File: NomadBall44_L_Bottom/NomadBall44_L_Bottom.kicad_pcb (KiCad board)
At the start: 2 copper layers, 149 x 96.5 mm, 58 parts, among them SW1 SW_Push, SW10 SW_Push, SW11 SW_Push, SW12 SW_Push, SW13 SW_Push, SW14 SW_Push, SW15 SW_Push, SW16 SW_Push, SW17 SW_Push, SW18 SW_Push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

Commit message: ボトムプレートを作成
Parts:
- removed BT1: Battery_Cell, NomadBall44:JST_S2B-PH-SM4-TB
- removed D1, D10, D11, D12, D13, D14, D15, D16, D17, D18, D19, D2, D20, D21, D22, D23, D3, D4, D5, D6, D7, D8, D9: D, NomadBall44:Diode_SMD
- removed SW1, SW10, SW11, SW12, SW13, SW14, SW15, SW16, SW17, SW18, SW2, SW22, SW23, SW3, SW4, SW5, SW6, SW7, SW8, SW9: SW_Push, NomadBall44:Choc_v2_Hotswap_1u
- removed SW19, SW20, SW21: SW_Push, NomadBall44:Kailh_Choc_V1_Hotswap_thin_via
- removed SW24: SW_SPDT, NomadBall44:TGSW_MSK-12D19
- removed U1: XIAO-nRF52840-Plus-SMD, NomadBall44:XIAO-nRF52840-Plus-ver2
- REF** (x9): value MountingHole_4.3mm_M4 -> Val**; footprint MountingHole:MountingHole_4.3mm_M4 -> NomadBall44:m2_Screw_Hole_EdgeCuts
- moved REF** 79.6 mm to (74.0, 73.3)
- moved REF** 79.6 mm to (152.2, 108.1)
- moved REF** 79.6 mm to (73.9, 100.1)
- moved REF** 79.6 mm to (91.6, 111.6)
- moved REF** 79.6 mm to (152.0, 66.5)
- moved REF** 79.6 mm to (112.3, 50.8)
- moved REF** 79.6 mm to (152.0, 86.0)
- moved REF** 79.6 mm to (112.1, 99.9)
- moved REF** 79.6 mm to (179.7, 121.6)
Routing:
- net Row3: track 230.2 -> 0.00 mm, vias 15 -> 0
- net Col5: track 212.8 -> 0.00 mm, vias 9 -> 0
- net Row1: track 190.7 -> 0.00 mm, vias 21 -> 0
- net Row2: track 179.8 -> 0.00 mm, vias 14 -> 0
- net Row0: track 171.8 -> 0.00 mm, vias 12 -> 0
- net Col4: track 170.4 -> 0.00 mm, vias 1 -> 0
- net Col2: track 167.8 -> 0.00 mm, vias 7 -> 0
- net Col1: track 154.1 -> 0.00 mm, vias 11 -> 0
- net Col3: track 154.1 -> 0.00 mm, vias 3 -> 0
- net Col0: track 131.7 -> 0.00 mm, vias 9 -> 0
- net GND: track 47.4 -> 0.00 mm, vias 5 -> 0
- net Net-(BT1--): track 19.2 -> 0.00 mm, vias 1 -> 0
- net Net-(D1-A): track 19.1 -> 0.00 mm, vias 2 -> 0
- net Net-(D5-A): track 19.1 -> 0.00 mm, vias 2 -> 0
- net Net-(D2-A): track 19.1 -> 0.00 mm, vias 2 -> 0
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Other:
- board size 149 x 96.5 mm -> 149 x 93.1 mm

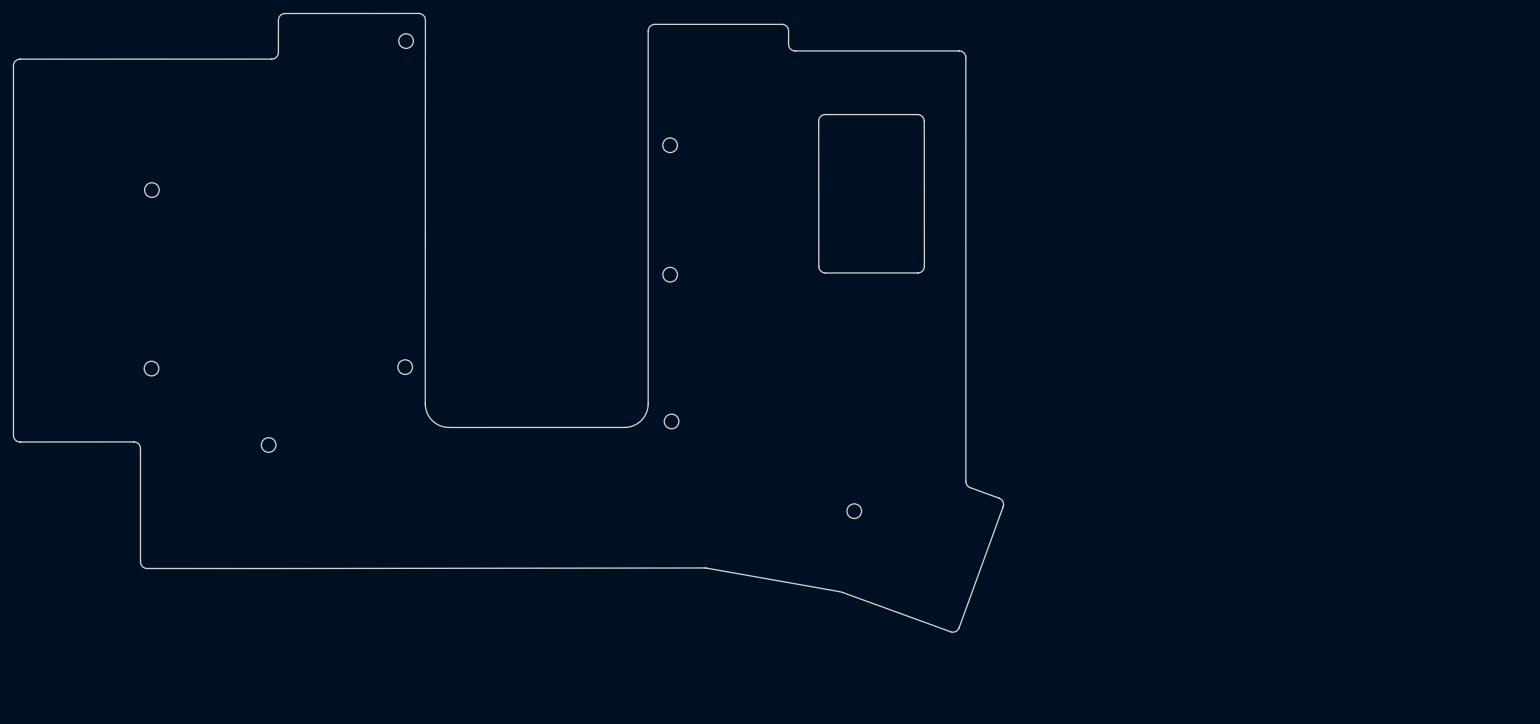
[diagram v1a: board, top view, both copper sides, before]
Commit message: ボトムプレートの位置を修正
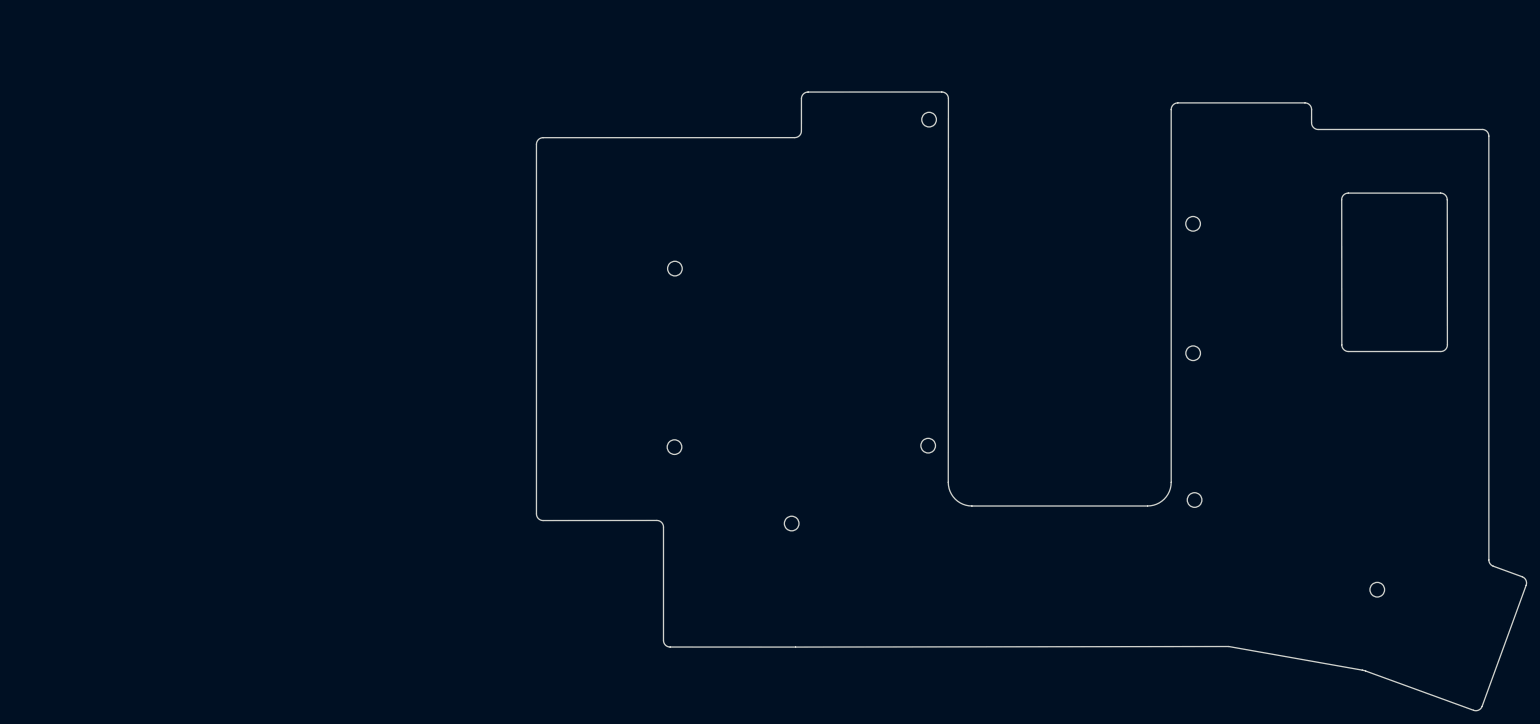
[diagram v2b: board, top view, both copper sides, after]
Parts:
- moved REF** 79.6 mm to (152.7, 85.1)
- moved REF** 79.6 mm to (230.9, 119.9)
- moved REF** 79.6 mm to (152.7, 112.0)
- moved REF** 79.6 mm to (170.3, 123.5)
- moved REF** 79.6 mm to (230.7, 78.3)
- moved REF** 79.6 mm to (191.0, 62.7)
- moved REF** 79.6 mm to (230.7, 97.8)
- moved REF** 79.6 mm to (190.8, 111.7)
- moved REF** 79.6 mm to (258.4, 133.4)
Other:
- outline, holes or cut-outs redrawn
